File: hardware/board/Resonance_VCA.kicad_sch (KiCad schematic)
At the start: 33 parts

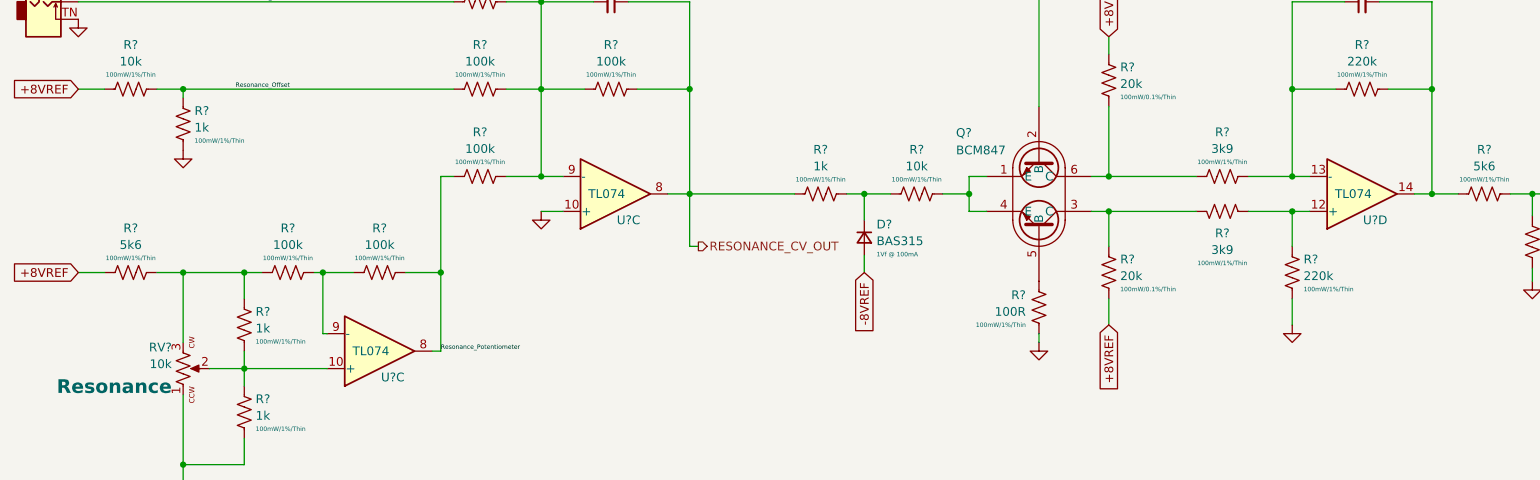
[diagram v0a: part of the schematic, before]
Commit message: hardware: finalize v3
- Updated version number and release date
- Swapped TL074C to TL074H
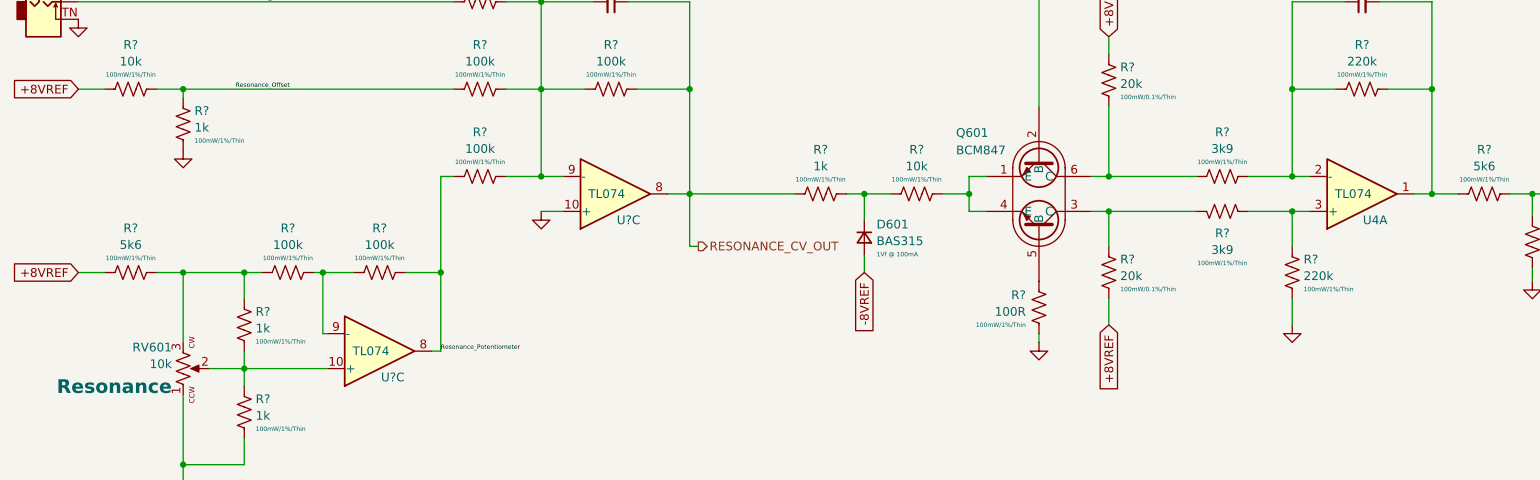
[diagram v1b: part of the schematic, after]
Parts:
- U4: renamed from U?; DigiKey 296-7198-1-ND -> 296-TL074HIPWRCT-ND; LCSC C96507 -> C4370424; MPN TL074CPWR -> TL074HIPWR; Notes (none) -> TL074H over TL074C due to better input offset voltage
- U? (x2): DigiKey 296-7198-1-ND -> 296-TL074HIPWRCT-ND; LCSC C96507 -> C4370424; MPN TL074CPWR -> TL074HIPWR; Notes (none) -> TL074H over TL074C due to better input offset voltage
- gave numbers to parts that had none: 3
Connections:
- net at C?.2, R?.1, R?.1: now also U4.1; no longer U4.14
- net at C?.1, R?.1, R?.2: now also U4.2 (-); no longer U4.13 (-)
- net at R?.1, R?.1: now also U4.3 (+); no longer U4.12 (+)
